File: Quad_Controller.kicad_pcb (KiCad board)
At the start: 4 copper layers, 47 x 47 mm, 44 parts, among them J1 Bat_Connect, J10 M1_Drive, J11 M2_Drive, J12 M3_Drive, J13 M4_Drive, J14 Conn_01x04_Female, J15 Conn_02x05_Odd_Even, J2 M1_VB, J3 M1_GND, J4 M2_VB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

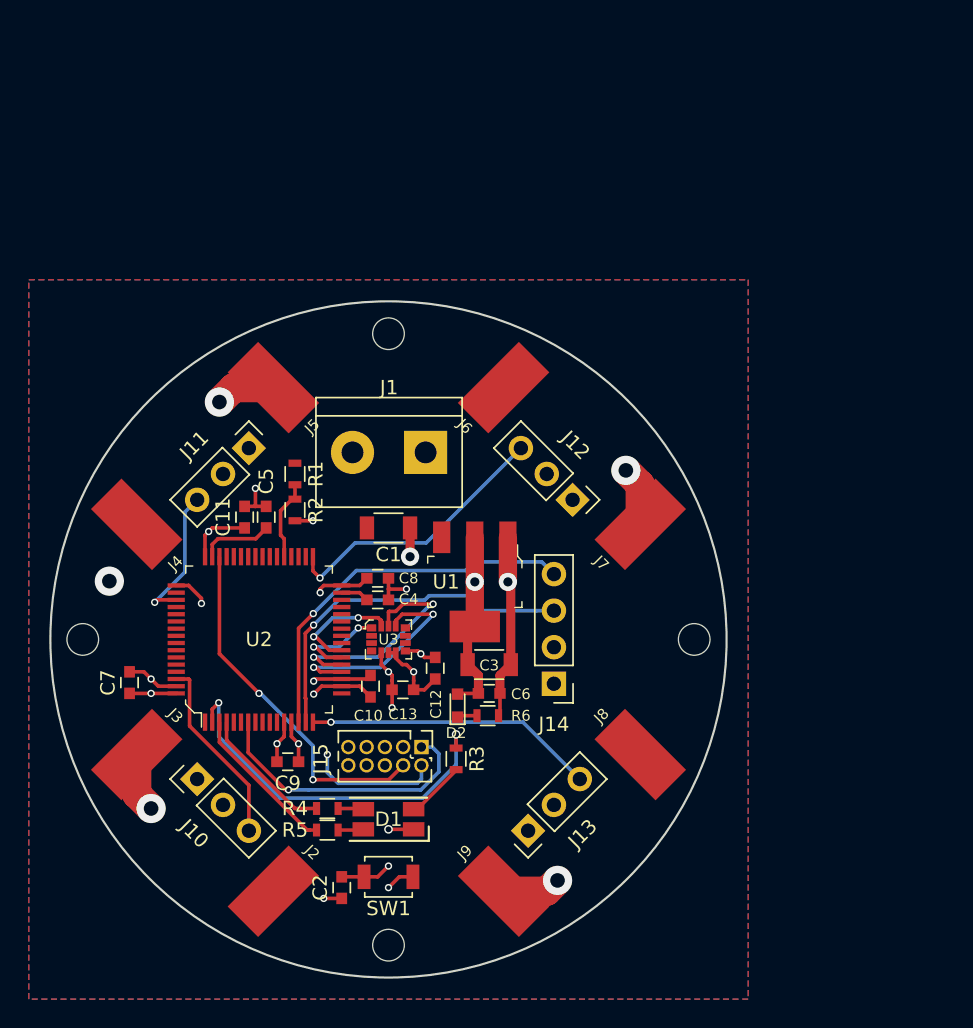
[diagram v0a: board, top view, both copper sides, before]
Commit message: Adding some small updates (redoing layout with components on back of board)
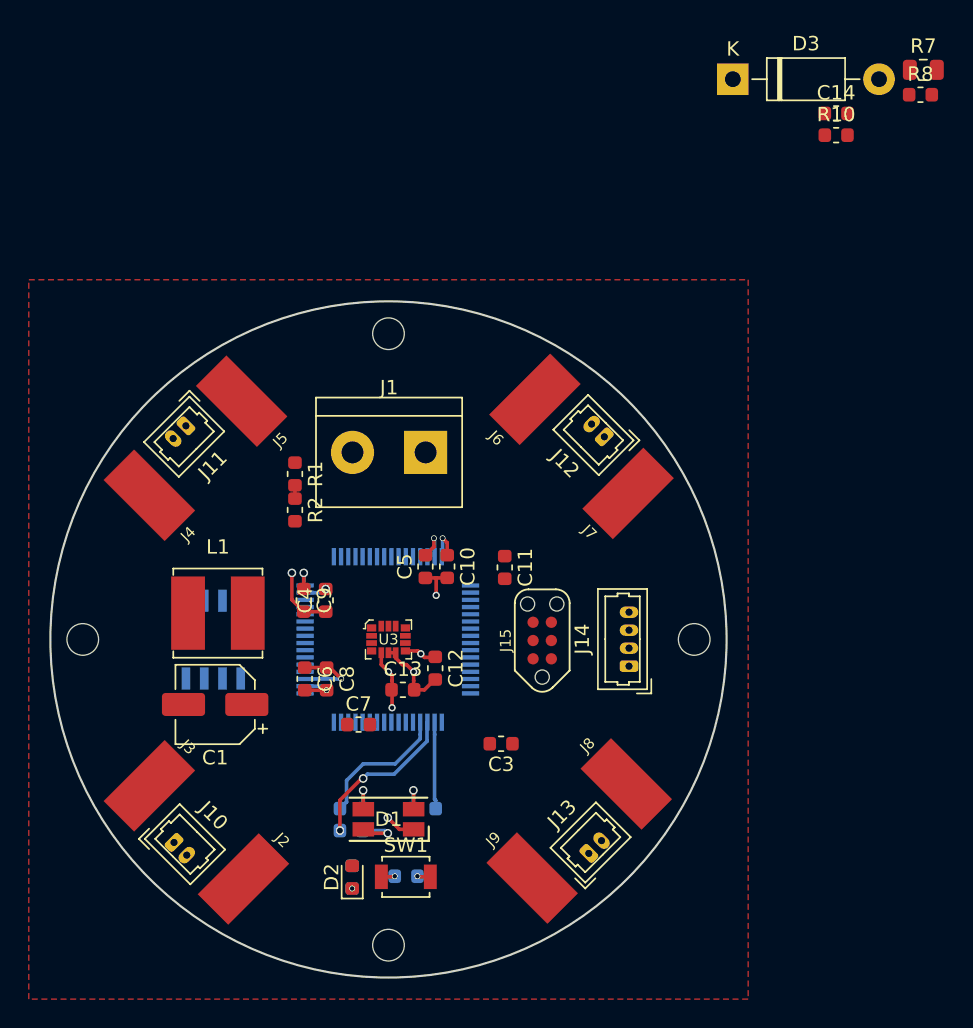
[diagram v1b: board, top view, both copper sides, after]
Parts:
- added C14: 470uF, Capacitor_SMD:C_0603_1608Metric, F.Cu at (171.1, 63.4)
- added D3: 1N5819, Diode_THT:D_DO-41_SOD81_P10.16mm_Horizontal, F.Cu at (163.9, 61.1)
- added L1: 220uH, Inductor_SMD:L_Bourns_SRN6045TA, F.Cu at (128.1, 98.2)
- added R10: 3.3k, Resistor_SMD:R_0603_1608Metric, F.Cu at (171.1, 65.0)
- added R7: 0.33, Resistor_SMD:R_0805_2012Metric, F.Cu at (177.2, 60.4)
- added R8: 2k, Resistor_SMD:R_0603_1608Metric, F.Cu at (177.0, 62.1)
- C1: value 10uF -> 100uF; footprint Capacitors_SMD:C_1206 -> Capacitor_SMD:CP_Elec_5x5.3
- C10, C11, C12, C13, C4, C5, C6, C7, C8, C9: footprint Capacitors_SMD:C_0603 -> Capacitor_SMD:C_0603_1608Metric
- C2: footprint Capacitors_SMD:C_0603 -> Capacitor_SMD:C_0603_1608Metric; moved to B.Cu
- C3: value 10uF -> 470pF; footprint Capacitors_SMD:C_1206 -> Capacitor_SMD:C_0603_1608Metric
- D1: footprint LEDs:LED_RGB_1210 -> LED_SMD:LED_RGB_1210
- D2: footprint LEDs:LED_0603 -> LED_SMD:LED_0603_1608Metric
- J1: footprint Connectors_Terminal_Blocks:TerminalBlock_bornier-2_P5.08mm -> TerminalBlock:TerminalBlock_bornier-2_P5.08mm
- J10, J11, J12, J13: footprint Pin_Headers:Pin_Header_Straight_1x03_Pitch2.54mm -> Connector_Molex:Molex_PicoBlade_53047-0210_1x02_P1.25mm_Vertical
- J14: footprint Socket_Strips:Socket_Strip_Straight_1x04_Pitch2.54mm -> Connector_Molex:Molex_PicoBlade_53047-0410_1x04_P1.25mm_Vertical
- J15: footprint Pin_Headers:Pin_Header_Straight_2x05_Pitch1.27mm -> Tag-Connect:TC2030-NL_SMALL
- R1, R2: footprint Resistors_SMD:R_0603 -> Resistor_SMD:R_0603_1608Metric
- R3, R4, R5, R6: footprint Resistors_SMD:R_0603 -> Resistor_SMD:R_0603_1608Metric; moved to B.Cu
- SW1: footprint Buttons_Switches_SMD:SW_SPST_B3U-1000P -> Button_Switch_SMD:SW_SPST_B3U-1000P
- U1: value LM1117MPX-3_3_NOPB -> MC34063AD; footprint digikey-footprints:SOT-223 -> Package_SO:SOIC-8_3.9x4.9mm_P1.27mm; moved to B.Cu
- U2: moved to B.Cu
- moved U1 18.6 mm to (127.8, 100.0), turned to 90 degrees
- moved C11 18.4 mm to (148.1, 95.0), turned to 270 degrees
- moved C1 17.2 mm to (128.0, 104.5)
- moved C7 16.2 mm to (137.9, 105.9), turned to 0 degrees
- moved R6 14.7 mm to (137.5, 116.5), turned to 90 degrees
- moved D2 14.0 mm to (137.5, 116.5)
- moved C6 12.9 mm to (134.2, 102.7), turned to 270 degrees
- moved C5 11.6 mm to (142.6, 94.9), turned to 90 degrees
- moved C9 11.3 mm to (134.1, 97.3), turned to 270 degrees
- moved J15 11.2 mm to (150.7, 100.1), turned to 90 degrees
- moved C10 9.88 mm to (144.1, 94.9)
- moved U2 8.95 mm to (140.0, 100.0), turned to 180 degrees
- moved C8 7.84 mm to (135.7, 102.7), turned to 270 degrees
- moved C3 5.56 mm to (147.8, 107.3)
- moved J14 5.36 mm to (156.7, 101.9), turned to 90 degrees
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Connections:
- C10 pad 2: GND -> GNDD
- C11 pad 2: GND -> GNDD
- C12 pad 2: GND -> GNDD
- C13 pad 1: VDD -> GNDD
- C13 pad 2: GND -> VDD
- C2 pad 1: GND -> GNDD
- C3 pad 1: GND -> Net-(C3-Pad1)
- C3 pad 2: VDD -> GNDD
- C4 pad 1: GND -> GNDD
- C5 pad 1: GND -> GNDD
- C6 pad 2: GND -> GNDD
- C7 pad 2: GND -> GNDD
- C8 pad 2: GND -> GNDD
- C9 pad 2: GND -> GNDD
- J10 pad 1: GND -> GNDD
- J10 pad 2: Net-(J10-Pad2) -> /M1S
- J11 pad 1: GND -> GNDD
- J11 pad 2: Net-(J11-Pad2) -> /M2S
- J12 pad 1: GND -> GNDD
- J12 pad 2: Net-(J12-Pad2) -> /M3S
- J13 pad 1: GND -> GNDD
- J13 pad 2: Net-(J13-Pad2) -> /M4S
- J14 pad 2: GND -> GNDD
- J15 pad 1: /RST -> VDD
- J15 pad 2: /SWCLK -> /SWDIO
- J15 pad 3: /SWIM -> /RST
- J15 pad 4: /SWDIO -> /SWCLK
- J15 pad 5: GND -> GNDD
- J15 pad 6: GND -> /SWIM
- R6 pad 2: GND -> GNDD
- SW1 pad 1: /RST -> GNDD
- SW1 pad 2: GND -> /RST
- U1 pad 1: GND -> Net-(R7-Pad1)
- U1 pad 2: VDD -> Net-(D3-Pad1)
- U1 pad 3: +12V -> Net-(C3-Pad1)
- U1 pad 4: VDD -> GNDD
- U2 pad 12: GND -> GNDD
- U2 pad 18: GND -> GNDD
- U2 pad 63: GND -> GNDD
- U3 pad 6: GND -> GNDD
- U3 pad 7: GND -> GNDD
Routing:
- net GND: track 58.1 -> 5.55 mm, vias 15 -> 1
- net /RST: track 32.3 -> 0.95 mm, vias 2 -> 1
- net /UART_TX: track 26.5 -> 0.00 mm, vias 1 -> 0
- net /SWCLK: track 25.8 -> 0.00 mm, vias 2 -> 0
- net /UART_RX: track 25.0 -> 0.00 mm, vias 1 -> 0
- net /SWDIO: track 24.9 -> 0.00 mm, vias 2 -> 0
- net +12V: track 23.1 -> 0.00 mm, vias 1 -> 0
- net VDD: track 39.6 -> 18.6 mm, vias 10 -> 7
- net /M4S: track 20.2 -> 0.00 mm, vias 1 -> 0
- net /RLED: track 26.2 -> 6.04 mm, vias 2 -> 0
- net /M3S: track 19.4 -> 0.00 mm, vias 1 -> 0
- net /SPI_CLK: track 16.3 -> 0.00 mm, vias 2 -> 0
- net /IMU_CS: track 15.4 -> 0.00 mm, vias 2 -> 0
- net /M1S: track 13.1 -> 0.00 mm
- net GNDD: track 0.00 -> 11.3 mm, vias 0 -> 4
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- removed copper zone on B.Cu, net GND

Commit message: Finished re-routing new design
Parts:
- C14, C3, R10, R7, R8: moved to B.Cu
- U1: moved to F.Cu
- moved R8 66.5 mm to (125.9, 104.7)
- moved R7 64.7 mm to (129.9, 104.6), turned to 180 degrees
- moved D3 60.3 mm to (122.9, 105.2), turned to 90 degrees
- moved R10 59.3 mm to (125.2, 102.5), turned to 270 degrees
- moved C14 59.2 mm to (126.7, 102.5), turned to 90 degrees
- moved C3 22.7 mm to (127.4, 97.3)
- moved C11 8.83 mm to (145.7, 103.5), turned to 90 degrees
- moved L1 7.74 mm to (130.9, 90.9)
- moved R1 7.60 mm to (139.2, 93.5)
- moved C1 4.95 mm to (130.7, 108.6), turned to 135 degrees
- moved R2 4.93 mm to (137.7, 93.5), turned to 90 degrees
- moved J1 4.83 mm to (137.9, 86.0), turned to 0 degrees
- moved C13 1.41 mm to (140.3, 102.3), turned to 180 degrees
- moved U1 0.95 mm to (128.8, 100.0), turned to 270 degrees
- moved C12 0.83 mm to (142.6, 101.5)
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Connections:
- U2 pad 16: /M4S -> /M1S
- U2 pad 33: /M3S -> /M2S
- U2 pad 51: /M2S -> /M3S
- U2 pad 62: /M1S -> /M4S
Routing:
- net /UART_RX: track 0.00 -> 28.5 mm, vias 0 -> 1
- net /UART_TX: track 0.00 -> 27.8 mm, vias 0 -> 1
- net /RST: track 0.95 -> 28.6 mm, vias 1 -> 3
- net Net-(D3-Pad1): track 0.00 -> 21.9 mm, vias 0 -> 2
- net GNDD: track 11.3 -> 32.0 mm, vias 4 -> 12
- net /M3S: track 0.00 -> 18.9 mm, vias 0 -> 1
- net /M2S: track 0.00 -> 16.5 mm, vias 0 -> 1
- net /M4S: track 0.00 -> 15.7 mm, vias 0 -> 1
- net /M1S: track 0.00 -> 14.7 mm, vias 0 -> 1
- net /SWDIO: track 0.00 -> 12.2 mm, vias 0 -> 2
- net /IMU_CS: track 0.00 -> 11.1 mm, vias 0 -> 1
- net /SPI_CLK: track 0.00 -> 9.95 mm, vias 0 -> 1
- net Net-(R7-Pad1): track 0.00 -> 8.68 mm, vias 0 -> 1
- net /SPI_MOSI: track 0.00 -> 8.32 mm, vias 0 -> 1
- net VDD: track 18.6 -> 26.0 mm, vias 7 -> 12
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- added copper zone on B.Cu, net GND
- added copper zone on In1.Cu, net GNDD
- removed copper zone on In1.Cu, net GND
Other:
- net class Default: clearance 0.2 -> 0.19812; via_dia 0.6 -> 0.6858; via_drill 0.4 -> 0.3302
- net class Power added: clearance 0.4, trace_width 1.27, via_dia 1.3716, via_drill 0.6604
- rule trace_clearance: 0.2 -> 0.19812
- rule trace_min: 0.2 -> 0.1524
- rule via_min_drill: 0.3 -> 0.3302
- rule via_min_size: 0.4 -> 0.6858

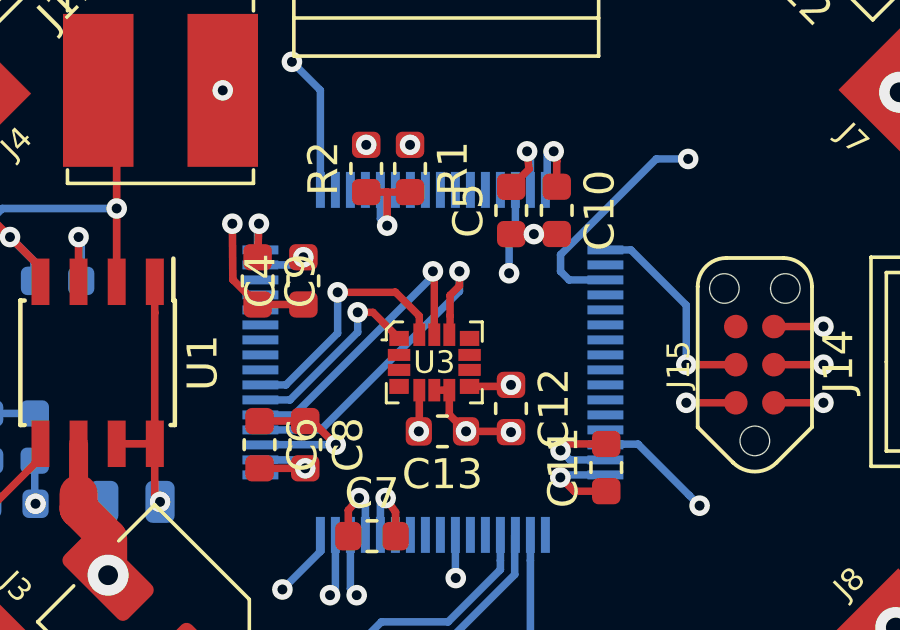
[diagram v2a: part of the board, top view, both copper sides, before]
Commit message: Connecting missed pad and clarifying formula for output of switching regulator)
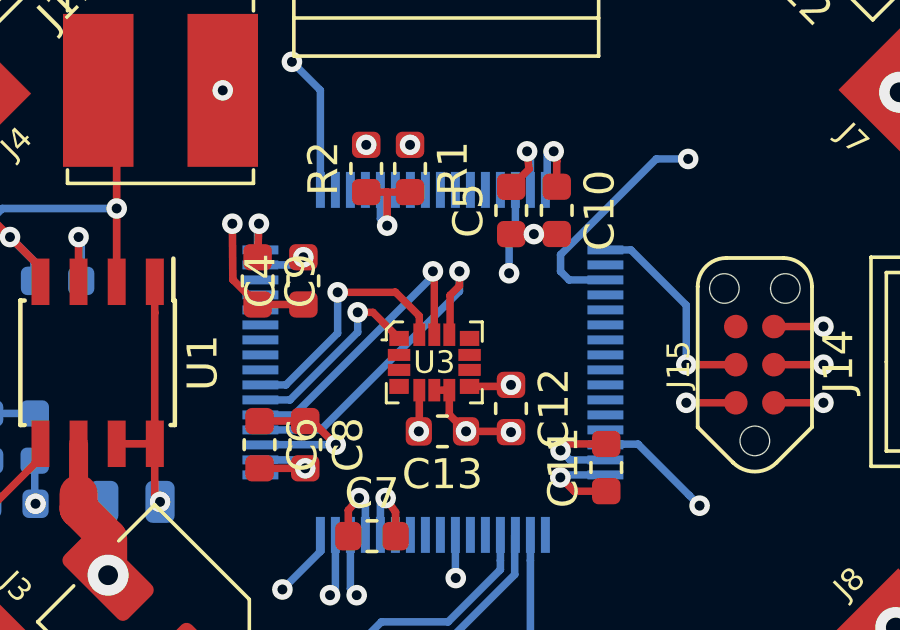
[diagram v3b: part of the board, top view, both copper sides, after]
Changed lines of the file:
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@@
-(kicad_pcb (version 20171130) (host pcbnew 5.0.2-bee76a0~70~ubuntu16.04.1)
+(kicad_pcb (version 20171130) (host pcbnew 5.1.2-f72e74a~84~ubuntu18.04.1)
   (general
     (thickness 1.6)
     (drawings 1)
-    (tracks 320)
+    (tracks 321)
     (zones 0)
     (modules 50)
@@
     (zone_45_only yes)
     (trace_min 0.1524)
-    (segment_width 0.2)
-    (edge_width 0.15)
     (via_size 0.6858)
     (via_drill 0.3302)
@@
     (uvia_min_size 0.2)
     (uvia_min_drill 0.1)
+    (edge_width 0.15)
+    (segment_width 0.2)
     (pcb_text_width 0.3)
     (pcb_text_size 1.5 1.5)
@@
   )
   (gr_circle (center 140 100) (end 163.5 100) (layer Edge.Cuts) (width 0.15))
-  (via (at 122.2375 88.773) (size 1.3716) (drill 0.6604) (layers F.Cu B.Cu) (net 2))
-  (via (at 124.5235 91.186) (size 1.3716) (drill 0.6604) (layers F.Cu B.Cu) (net 2))
   (via (at 128.5875 82.296) (size 1.3716) (drill 0.6604) (layers F.Cu B.Cu) (net 1))
   (via (at 131.0005 84.582) (size 1.3716) (drill 0.6604) (layers F.Cu B.Cu) (net 1))
-  (via (at 149.0345 84.455) (size 1.3716) (drill 0.6604) (layers F.Cu B.Cu) (net 2))
-  (via (at 151.384 82.2325) (size 1.3716) (drill 0.6604) (layers F.Cu B.Cu) (net 2))
   (via (at 157.7975 88.7095) (size 1.3716) (drill 0.6604) (layers F.Cu B.Cu) (net 1))
   (via (at 155.5115 90.9955) (size 1.3716) (drill 0.6604) (layers F.Cu B.Cu) (net 1))
-  (via (at 155.3845 108.839) (size 1.3716) (drill 0.6604) (layers F.Cu B.Cu) (net 2))
-  (via (at 157.6705 111.252) (size 1.3716) (drill 0.6604) (layers F.Cu B.Cu) (net 2))
   (via (at 151.0665 117.729) (size 1.3716) (drill 0.6604) (layers F.Cu B.Cu) (net 1))
   (via (at 148.9075 115.443) (size 1.3716) (drill 0.6604) (layers F.Cu B.Cu) (net 1))
   (via (at 124.5235 108.966) (size 1.3716) (drill 0.6604) (layers F.Cu B.Cu) (net 1))
   (via (at 122.2375 111.3155) (size 1.3716) (drill 0.6604) (layers F.Cu B.Cu) (net 1))
-  (via (at 131.064 115.5065) (size 1.3716) (drill 0.6604) (layers F.Cu B.Cu) (net 2))
-  (via (at 128.778 117.7925) (size 1.3716) (drill 0.6604) (layers F.Cu B.Cu) (net 2))
   (via (at 132.238635 110.204135) (size 1.3716) (drill 0.6604) (layers F.Cu B.Cu) (net 1))
   (via (at 123.3805 110.1725) (size 1.3716) (drill 0.6604) (layers F.Cu B.Cu) (net 1))
@@
   (via (at 129.794 83.439) (size 1.3716) (drill 0.6604) (layers F.Cu B.Cu) (net 1))
   (via (at 137.7315 92.748) (size 0.6858) (drill 0.3302) (layers F.Cu B.Cu) (net 1))
+  (via (at 122.2375 88.773) (size 1.3716) (drill 0.6604) (layers F.Cu B.Cu) (net 2))
+  (via (at 124.5235 91.186) (size 1.3716) (drill 0.6604) (layers F.Cu B.Cu) (net 2))
+  (via (at 149.0345 84.455) (size 1.3716) (drill 0.6604) (layers F.Cu B.Cu) (net 2))
+  (via (at 151.384 82.2325) (size 1.3716) (drill 0.6604) (layers F.Cu B.Cu) (net 2))
+  (via (at 155.3845 108.839) (size 1.3716) (drill 0.6604) (layers F.Cu B.Cu) (net 2))
+  (via (at 157.6705 111.252) (size 1.3716) (drill 0.6604) (layers F.Cu B.Cu) (net 2))
+  (via (at 131.064 115.5065) (size 1.3716) (drill 0.6604) (layers F.Cu B.Cu) (net 2))
+  (via (at 128.778 117.7925) (size 1.3716) (drill 0.6604) (layers F.Cu B.Cu) (net 2))
   (segment (start 129.127365 105.861494) (end 128.143 104.877129) (width 1.27) (layer F.Cu) (net 2))
   (segment (start 128.143 104.877129) (end 128.143 104.380502) (width 1.27) (layer F.Cu) (net 2))
@@
   (segment (start 136.220006 102.25) (end 140.839803 97.630203) (width 0.25) (layer B.Cu) (net 64))
   (segment (start 134.204 102.25) (end 136.220006 102.25) (width 0.25) (layer B.Cu) (net 64))
-  (segment (start 140.525001 97.764235) (end 140.525001 98.439999) (width 0.25) (layer F.Cu) (net 64))
-  (segment (start 140.525001 98.439999) (end 140.525001 98.689997) (width 0.25) (layer F.Cu) (net 64))
+  (segment (start 140.523121 99.051879) (end 140.523121 99.075) (width 0.25) (layer F.Cu) (net 64))
+  (segment (start 140.525001 99.049999) (end 140.523121 99.051879) (width 0.25) (layer F.Cu) (net 64))
+  (segment (start 140.525001 97.764235) (end 140.525001 99.049999) (width 0.25) (layer F.Cu) (net 64))
   (segment (start 140.839803 97.449433) (end 140.525001 97.764235) (width 0.25) (layer F.Cu) (net 64))
   (segment (start 140.839803 96.9645) (end 140.839803 97.449433) (width 0.25) (layer F.Cu) (net 64))
